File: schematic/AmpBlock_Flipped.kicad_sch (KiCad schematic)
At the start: 13 parts, among them IC24 LTC6090CS8E#PBF

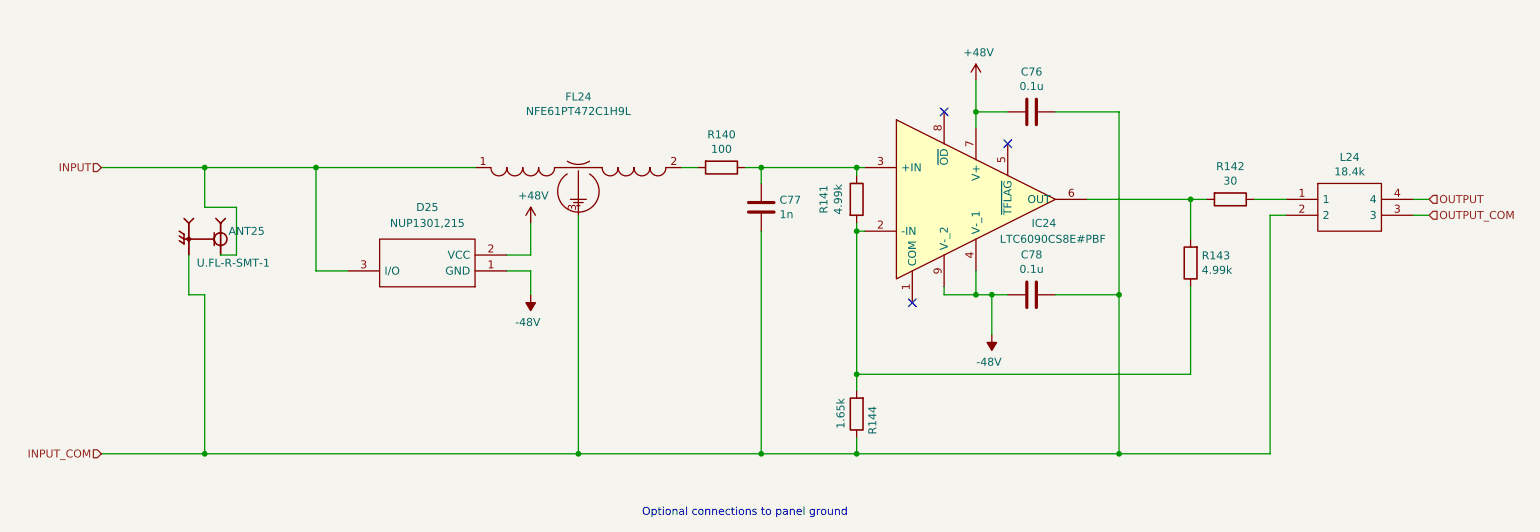
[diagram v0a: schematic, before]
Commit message: Update board design to better support enclosure with fan connect and diode connect headers. Also widen differential choke land pads and include enclosure CAD.
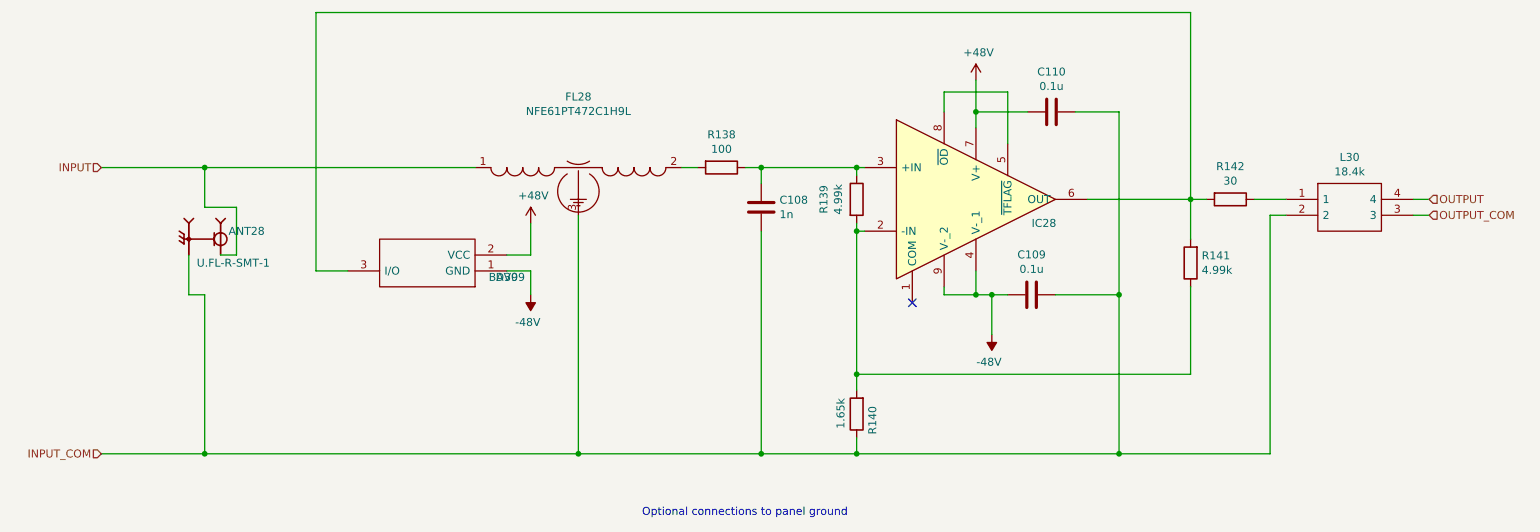
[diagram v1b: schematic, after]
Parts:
- ANT28: renamed from ANT25; AVAILABILITY Y -> (none); Availability (none) -> Y; MANUFACTURER Hirose -> (none); MPN (none) -> U.FL-R-SMT(10); Manufacturer (none) -> Hirose; Manufacturer_Part_Number U.FL-R-SMT(10) -> (none); Type (none) -> SMT
- C108: renamed from C77; AVAILABILITY Y -> (none); Availability (none) -> Y; MANUFACTURER Samsung -> (none); MPN (none) -> CL10B102KC8NNNC; Manufacturer (none) -> Samsung; Manufacturer_Part_Number CL10B102KC8NNNC -> (none); Package (none) -> 0603; Type (none) -> SMT
- C109: renamed from C78; AVAILABILITY Y -> (none); Availability (none) -> Y; MPN (none) -> CL10B104KC8NNNC; Manufacturer_Part_Number CL10B104KC8NNNC -> (none)
- C110: renamed from C76; AVAILABILITY Y -> (none); Availability (none) -> Y; MANUFACTURER Samsung -> (none); MPN (none) -> CL10B104KC8NNNC; Manufacturer (none) -> Samsung; Manufacturer_Part_Number CL10B104KC8NNNC -> (none)
- D30: renamed from D25; value NUP1301,215 -> BAV99; AVAILABILITY Y -> (none); Availability (none) -> Y; Digikey Number 1727-5056-2-ND -> 264-BAV99LMTR-ND; MANUFACTURER Nexperia -> (none); MPN (none) -> BAV99,LM; Manufacturer (none) -> Toshiba; Manufacturer_Part_Number NUP1301,215 -> (none); Type (none) -> SMT
- FL28: renamed from FL24; AVAILABILITY Y -> (none); Availability (none) -> Y; MANUFACTURER Murata Electronics -> (none); MPN (none) -> NFE61PT472C1H9L; Manufacturer (none) -> Murata Electronics; Manufacturer_Part_Number NFE61PT472C1H9L -> (none); Package (none) -> 2706, 3 PC Pad; Type (none) -> SMT
- IC28: renamed from IC24; value LTC6090CS8E#PBF -> (none); AVAILABILITY Y -> (none); Availability (none) -> Y; MANUFACTURER Analog Devices Inc. -> (none); MPN (none) -> LTC6090CS8E#PBF; Manufacturer (none) -> Analog Devices Inc.; Manufacturer_Part_Number LTC6090CS8E#PBF -> (none); Package (none) -> SOIC-8E; Type (none) -> SMT
- L30: renamed from L24; footprint ARTIQAmp:WE-SL2 -> ARTIQAmp:WE-SL2-WIDE; AVAILABILITY Y -> (none); Availability (none) -> Y; MANUFACTURER Wurth Elektronik -> (none); MPN (none) -> 744229; Manufacturer (none) -> Wurth Elektronik; Manufacturer_Part_Number 744229 -> (none); Type (none) -> SMT
- R138: renamed from R140; AVAILABILITY Y -> (none); Availability (none) -> Y; MPN (none) -> RMCF0603FG100R; Manufacturer_Part_Number RMCF0603FG100R -> (none)
- R139: renamed from R141; AVAILABILITY Y -> (none); Availability (none) -> Y; MANUFACTURER Stackpole Electronics Inc -> (none); MPN (none) -> RMCF0603FT4K99; Manufacturer (none) -> Stackpole Electronics Inc; Manufacturer_Part_Number RMCF0603FT4K99 -> (none)
- R140: renamed from R144; AVAILABILITY Y -> (none); Availability (none) -> Y; MANUFACTURER Stackpole Electronics Inc -> (none); MPN (none) -> RMCF0603FT1K65; Manufacturer (none) -> Stackpole Electronics Inc; Manufacturer_Part_Number RMCF0603FT1K65 -> (none); Type (none) -> SMT
- R141: renamed from R143; AVAILABILITY Y -> (none); Availability (none) -> Y; MANUFACTURER Stackpole Electronics Inc -> (none); MPN (none) -> RMCF0603FT4K99; Manufacturer (none) -> Stackpole Electronics Inc; Manufacturer_Part_Number RMCF0603FT4K99 -> (none)
- R142: AVAILABILITY Y -> (none); Availability (none) -> Y; MANUFACTURER Stackpole Electronics Inc -> (none); MPN (none) -> RMCF0603FT30R0; Manufacturer (none) -> Stackpole Electronics Inc; Manufacturer_Part_Number RMCF0603FT30R0 -> (none)
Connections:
- net INPUT: no longer D30.3 (I/O)
- net at IC28.6 (OUT), R141.2, R142.2: now also D30.3 (I/O)
- net at IC28.5 (~{TFLAG}): now also IC28.8 (~{OD})
- no-connect marks 3 -> 1
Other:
- moved on the sheet: C110
